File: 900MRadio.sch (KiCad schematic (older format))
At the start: 59 parts, among them P3 BNC, P4 BNC, U3 CC1200, U4 CC1190, U6 0900PC15J0013, U7 EPCOS_B3588, X2 FA-20H32.0000MF20X-K3

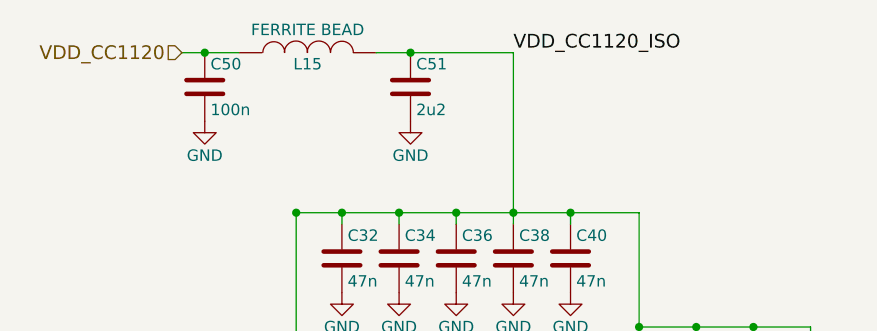
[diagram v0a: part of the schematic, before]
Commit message: Added capacitors for XMC chip, diagram of power tree, and more connectors.
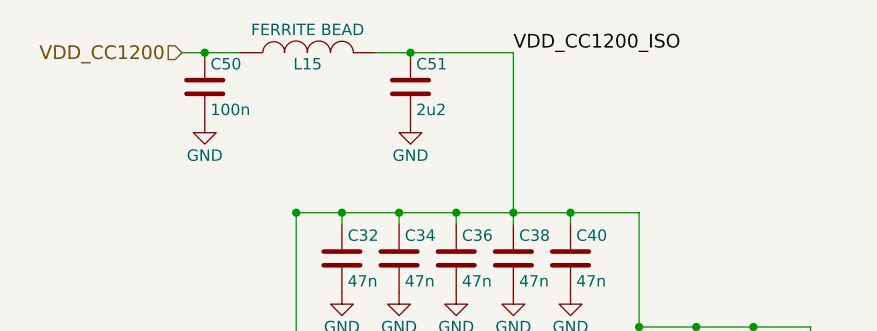
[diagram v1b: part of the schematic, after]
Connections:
- net VDD_CC1120 renamed VDD_CC1200
- net VDD_CC1120_ISO renamed VDD_CC1200_ISO

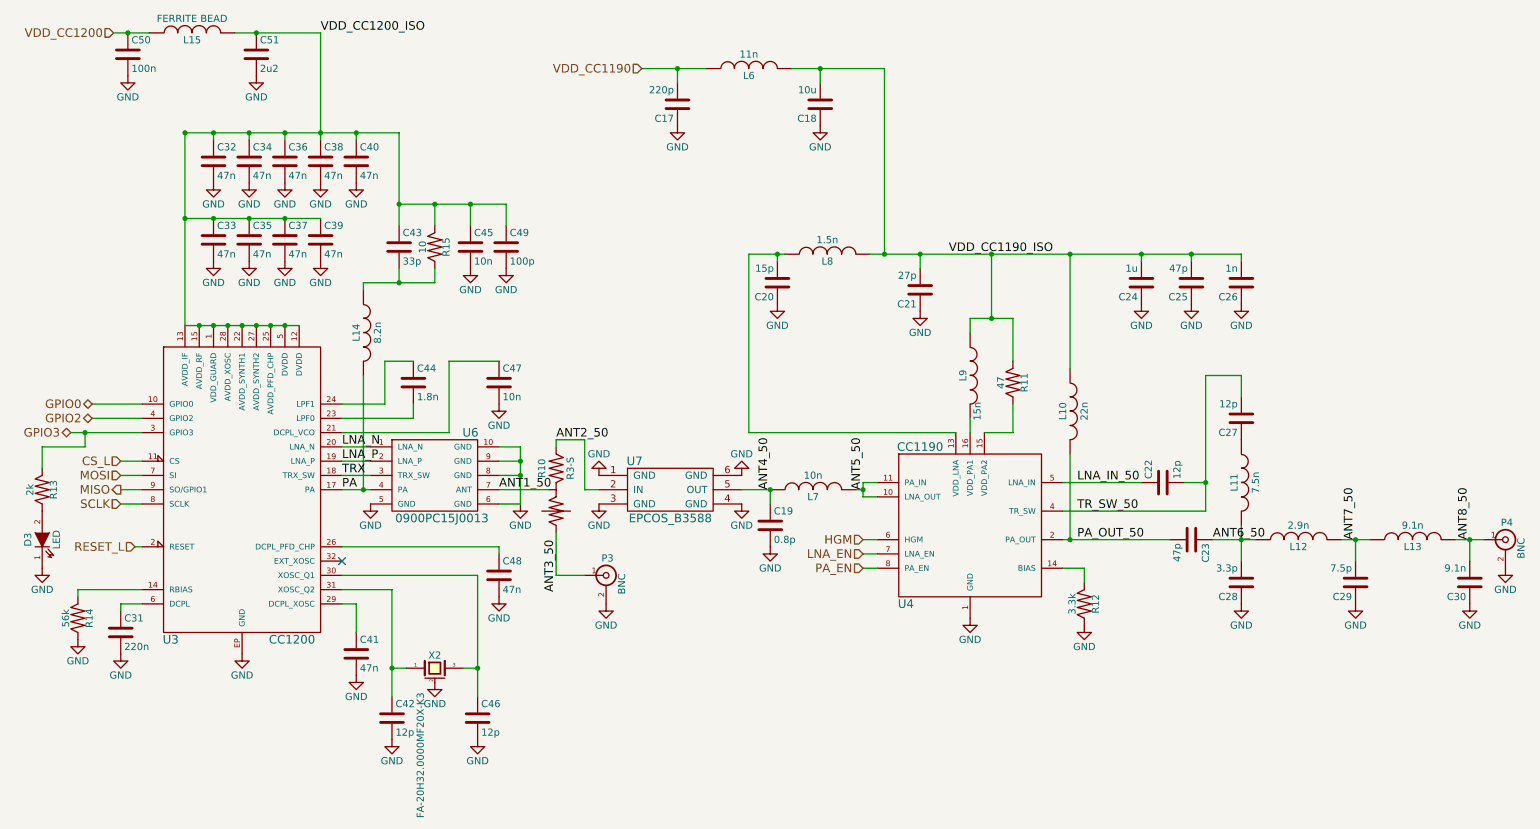
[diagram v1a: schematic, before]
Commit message: Added 3.3V LDO
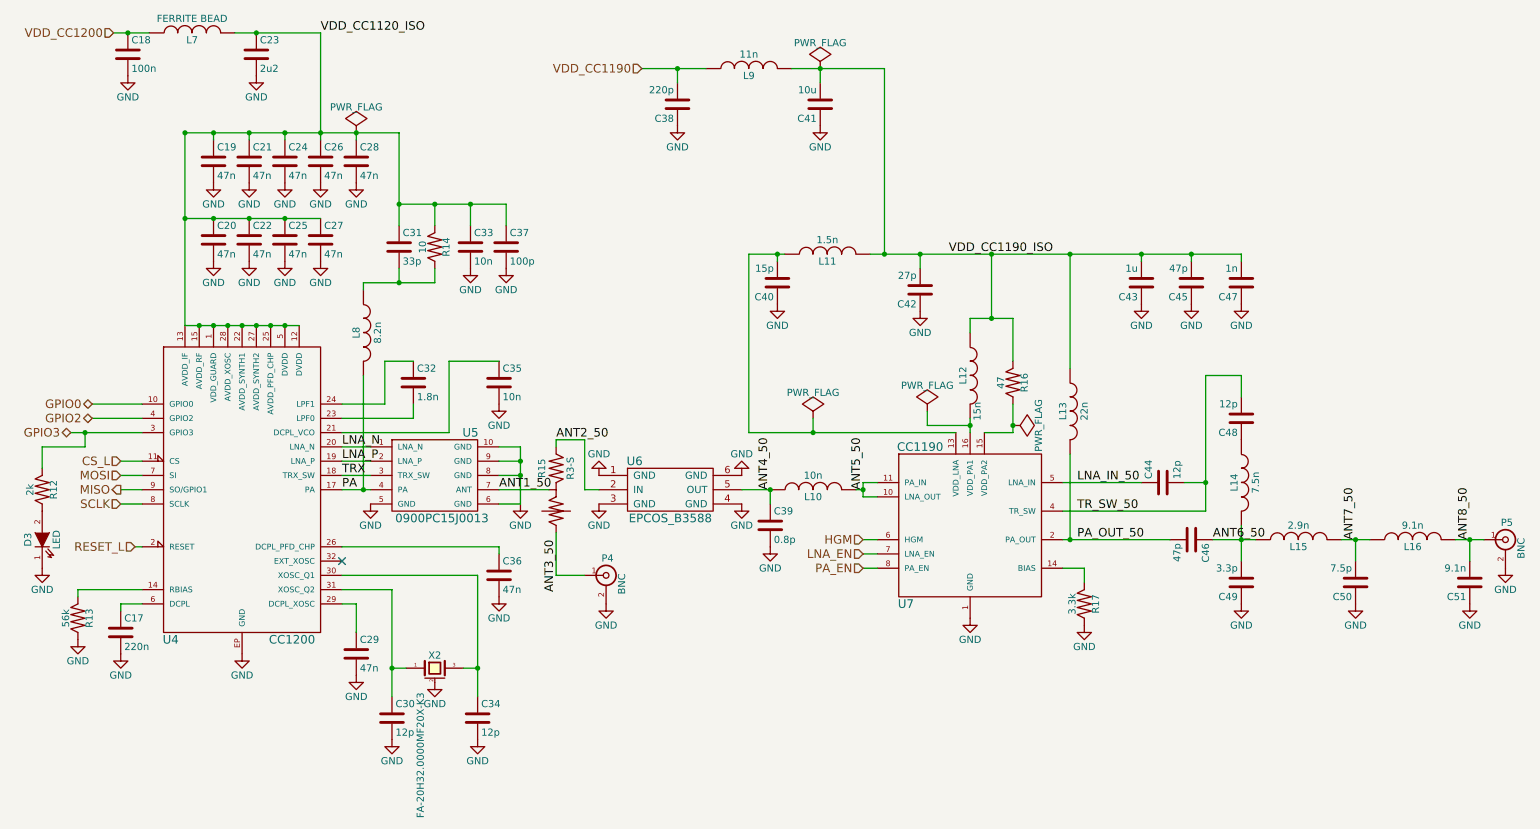
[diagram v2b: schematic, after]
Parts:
- removed U7: EPCOS_B3588, SMD_Packages:DCC6C, symbol EPCOS_B3588
- added U6: EPCOS_B3588, SMD_Packages:DCC6C, symbol EPCOS_B3588
- renumbered C31 to C17, C50 to C18, C32 to C19, C33 to C20, C34 to C21, C35 to C22, C51 to C23, C36 to C24, C37 to C25, C38 to C26, C39 to C27, C40 to C28, C41 to C29, C42 to C30, C43 to C31, C44 to C32, C45 to C33, C46 to C34, C47 to C35, C48 to C36, C49 to C37, C17 to C38, C19 to C39, C20 to C40, C18 to C41, C21 to C42, C24 to C43, C22 to C44, C25 to C45, C23 to C46, C26 to C47, C27 to C48, C28 to C49, C29 to C50, C30 to C51, L7 to L10, L8 to L11, L9 to L12, L10 to L13, L11 to L14, L12 to L15, L13 to L16, L15 to L7, L14 to L8, L6 to L9, P3 to P4, P4 to P5, R13 to R12, R14 to R13, R15 to R14, R10 to R15, R11 to R16, R12 to R17, U3 to U4, U6 to U5, U4 to U7
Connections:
- net ANT2_50: now also U6.2 (IN)
- net ANT4_50: now also U6.5 (OUT)
- net GND: now also U6.1 (GND), U6.3 (GND), U6.4 (GND), U6.6 (GND)
- net VDD_CC1200_ISO renamed VDD_CC1120_ISO
